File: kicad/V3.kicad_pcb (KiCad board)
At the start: 2 copper layers, 161.3 x 118.3 mm, 48 parts, among them U1 SuperMini nRF52840

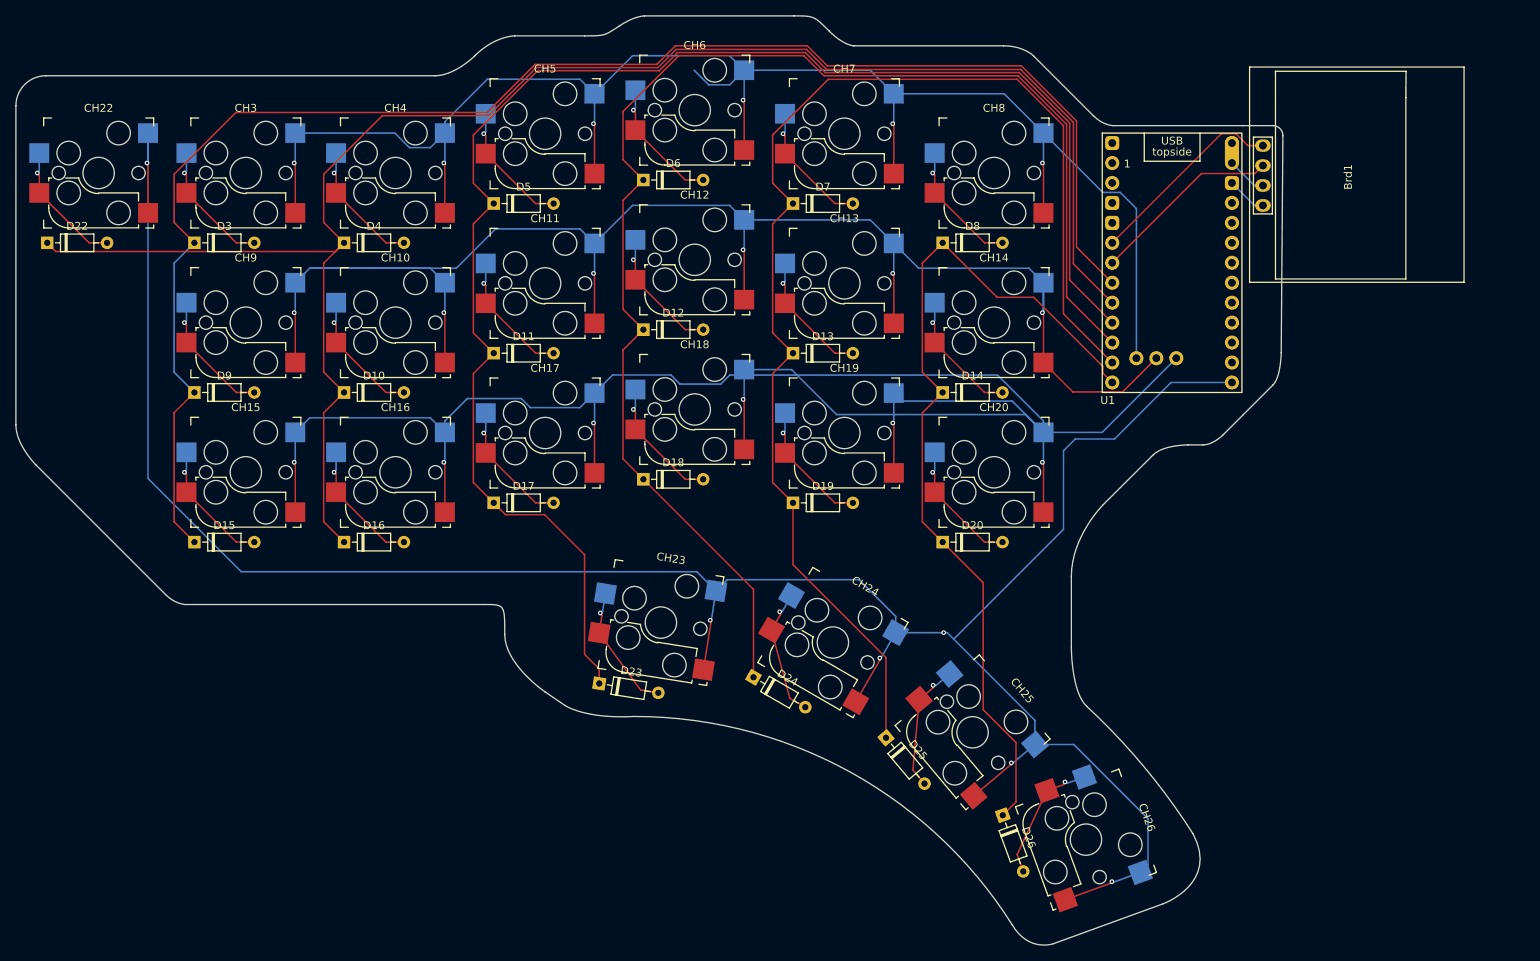
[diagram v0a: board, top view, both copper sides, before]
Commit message: change to esp32
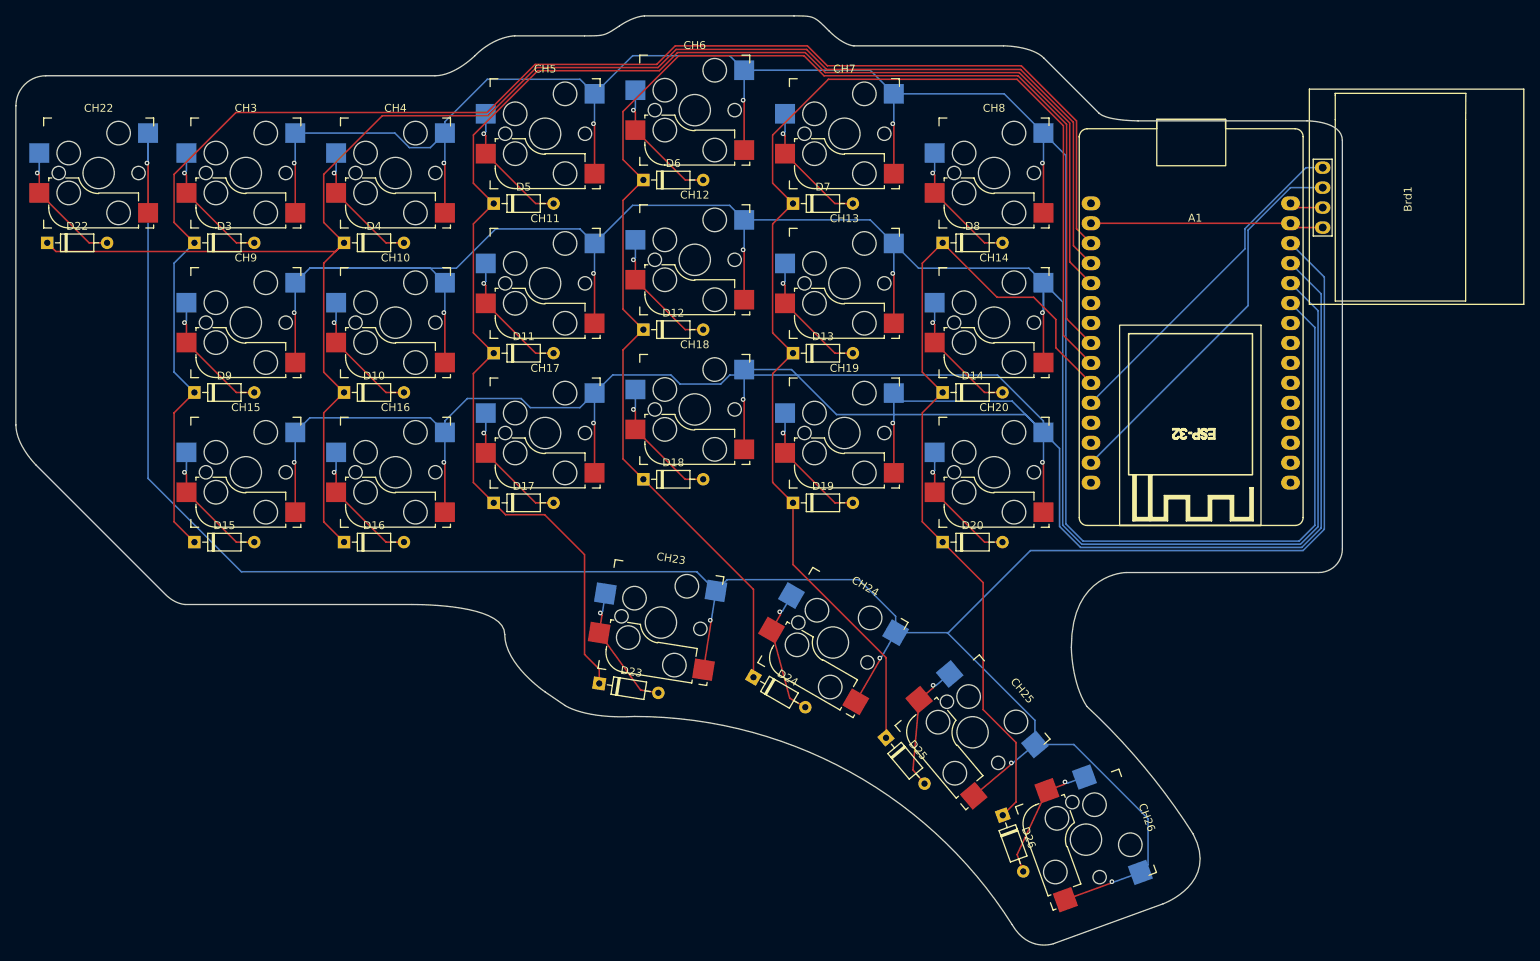
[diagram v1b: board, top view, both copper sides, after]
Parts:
- removed U1: SuperMini nRF52840, PCM_marbastlib-xp-promicroish:SuperMini_nRF52840_AH_USBup
- added A1: ESP32_DevKit_V1_DOIT_30GPIOs, PCM_SL_Development_Boards:DOIT_ESP32_DEVKIT_30Pins, F.Cu at (197.5, 64.5)
- moved Brd1 8.11 mm to (237.6, 64.0)
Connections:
- Brd1 pad 3: SDA -> SCL
- Brd1 pad 4: SDL -> SDA
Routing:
- net Row2: track 206.2 -> 287.2 mm
- net Row1: track 211.7 -> 282.9 mm
- net Row3: track 251.4 -> 314.2 mm
- net SCL: track 0.00 -> 49.6 mm
- net Row4: track 306.8 -> 343.7 mm, vias 6 -> 5
- net SDL: track 25.6 -> 0.00 mm
- net Earth: track 5.13 -> 29.7 mm
- net SDA: track 24.3 -> 43.4 mm
- net Col3: track 195.3 -> 189.2 mm
- net Col2: track 221.8 -> 215.6 mm
- net Col1: track 200.3 -> 194.1 mm
- net Col6: track 111.2 -> 110.1 mm
- net Col5: track 162.1 -> 161.1 mm
- net Col4: track 176.4 -> 175.4 mm
- net VCC: track 5.13 -> 4.32 mm
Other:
- board size 161.3 x 118.3 mm -> 168.9 x 118.3 mm

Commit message: problematic diodes
d2 and d34 cannot be used,d2 is the same pin as the builtin led, which
is used for serial confirmation rn, and d34 is input only
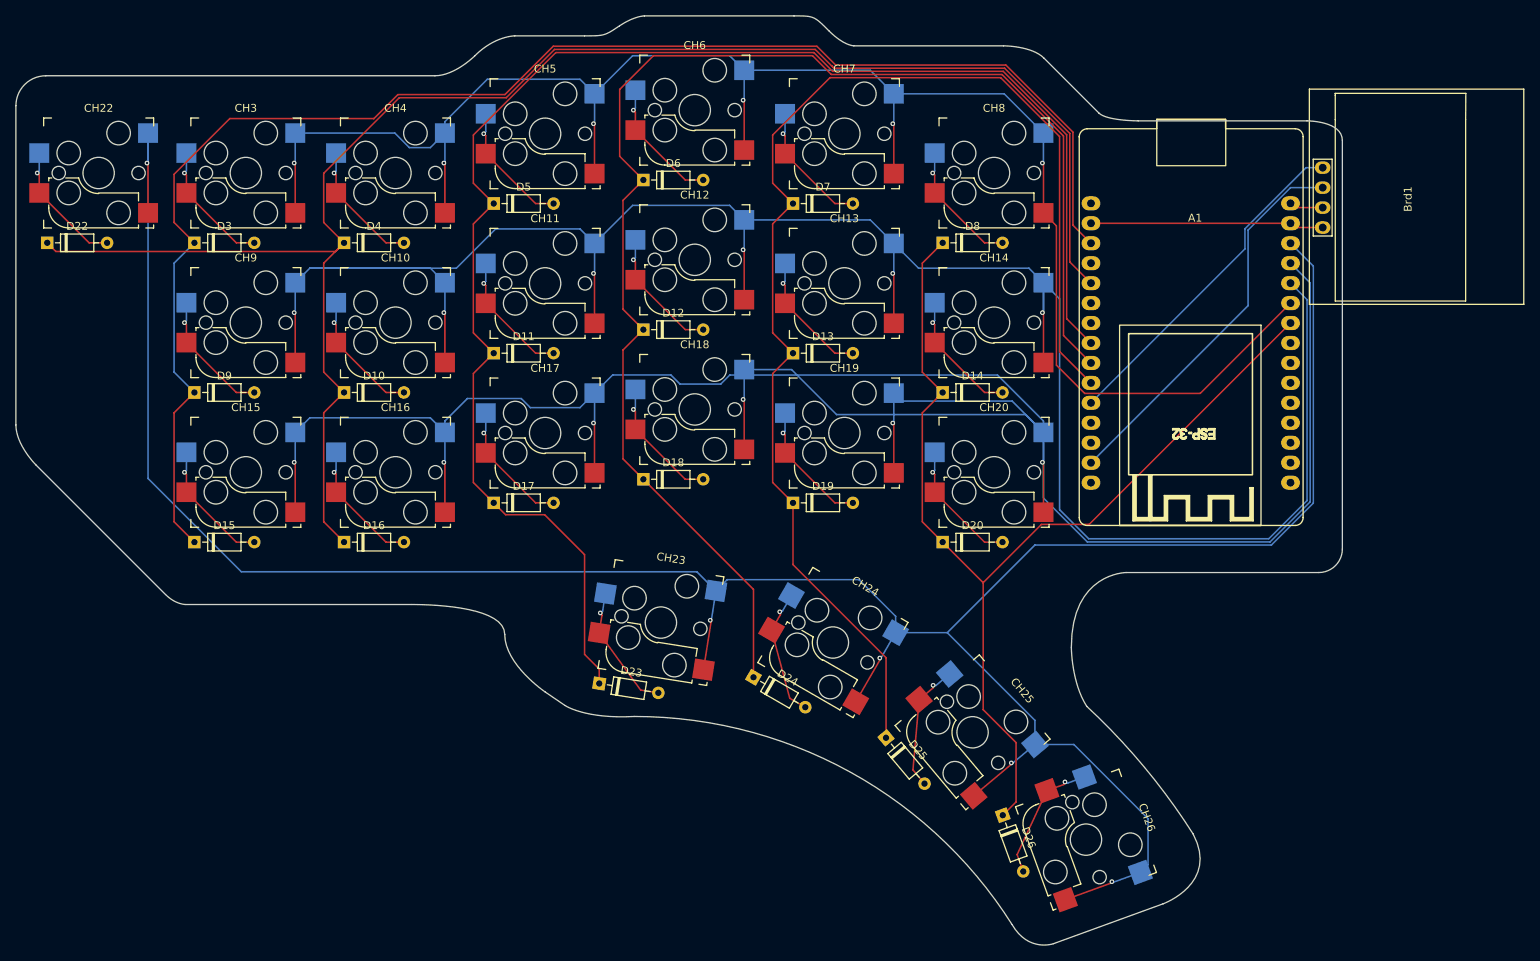
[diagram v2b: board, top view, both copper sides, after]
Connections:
- A1 pad 10: Col6 -> Col5
- A1 pad 24: unconnected-(A1-DAC2/ADC2_CH9/D26-Pad24) -> Col6
- A1 pad 4: Col2 -> unconnected-(A1-D2/ADC2_CH2-Pad4)
- A1 pad 5: Col3 -> Col2
- A1 pad 8: Col4 -> Col3
- A1 pad 9: Col5 -> Col4
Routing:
- net Row1: track 282.9 -> 225.1 mm
- net Col6: track 110.1 -> 134.5 mm
- net Col3: track 189.2 -> 195.7 mm
- net Row2: track 287.2 -> 281.8 mm
- net Row3: track 314.2 -> 308.8 mm
- net Row4: track 343.7 -> 339.7 mm
- net Col4: track 175.4 -> 179.0 mm
- net Col2: track 215.6 -> 217.3 mm
- net Col5: track 161.1 -> 162.7 mm
- net Col1: track 194.1 -> 193.0 mm

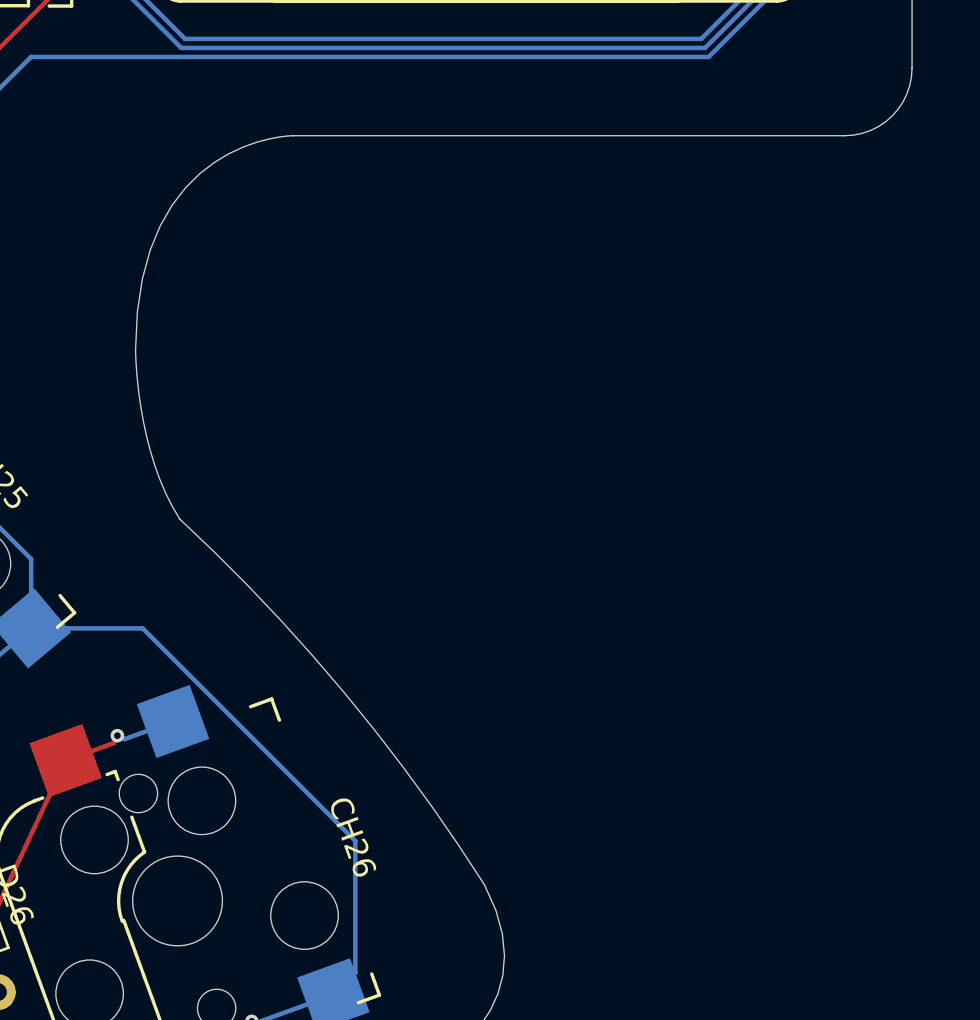
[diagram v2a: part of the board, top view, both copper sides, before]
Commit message: change from global to sheet labels
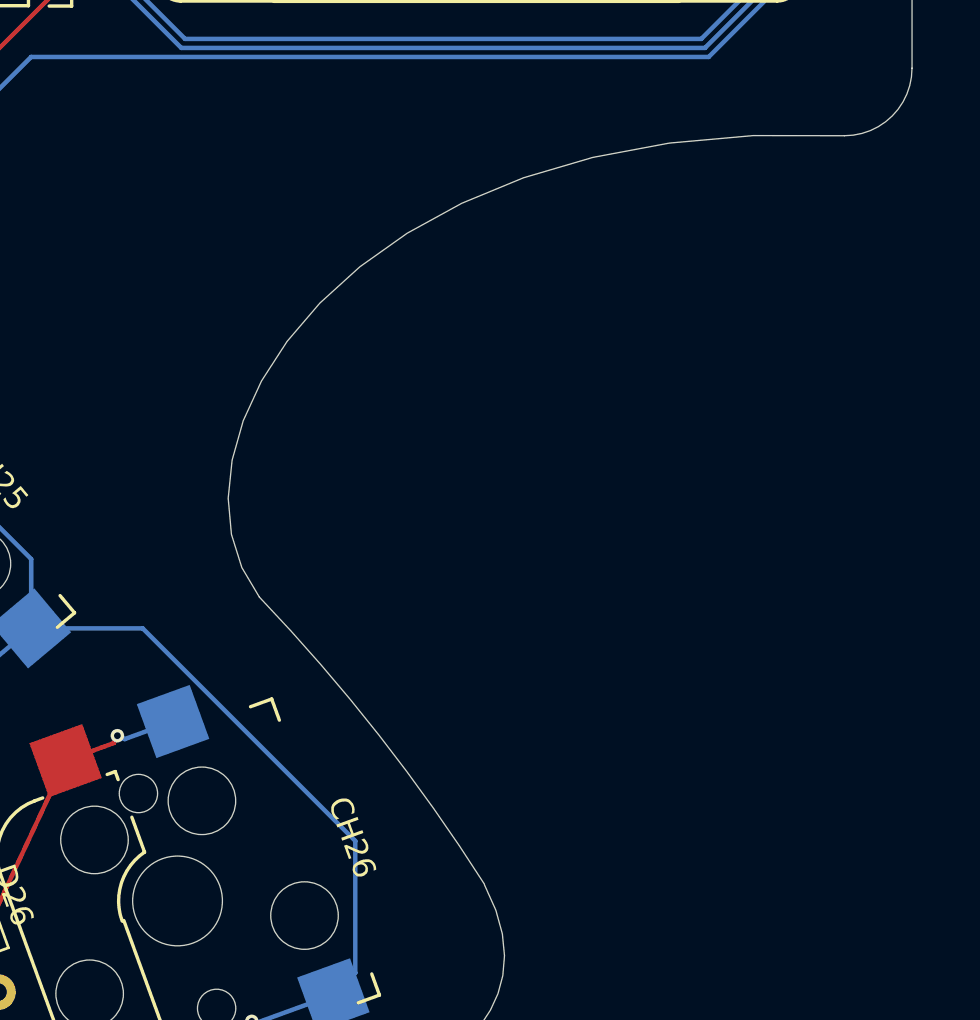
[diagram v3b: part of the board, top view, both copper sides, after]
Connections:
- net Col1 renamed /Col1
- net Col2 renamed /Col2
- net Col3 renamed /Col3
- net Col4 renamed /Col4
- net Col5 renamed /Col5
- net Col6 renamed /Col6
- net Row1 renamed /Row1
- net Row2 renamed /Row2
- net Row3 renamed /Row3
- net Row4 renamed /Row4
- A1 pad 11: SDA -> unconnected-(A1-D21/SDA-Pad11)
- A1 pad 14: SCL -> unconnected-(A1-D22/SCL-Pad14)
- Brd1 pad 3: SCL -> /SCL
- Brd1 pad 4: SDA -> /SDA
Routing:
- net (no net): track 0.00 -> 93.0 mm
- net SCL: track 49.6 -> 0.00 mm
- net SDA: track 43.4 -> 0.00 mm
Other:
- outline, holes or cut-outs redrawn

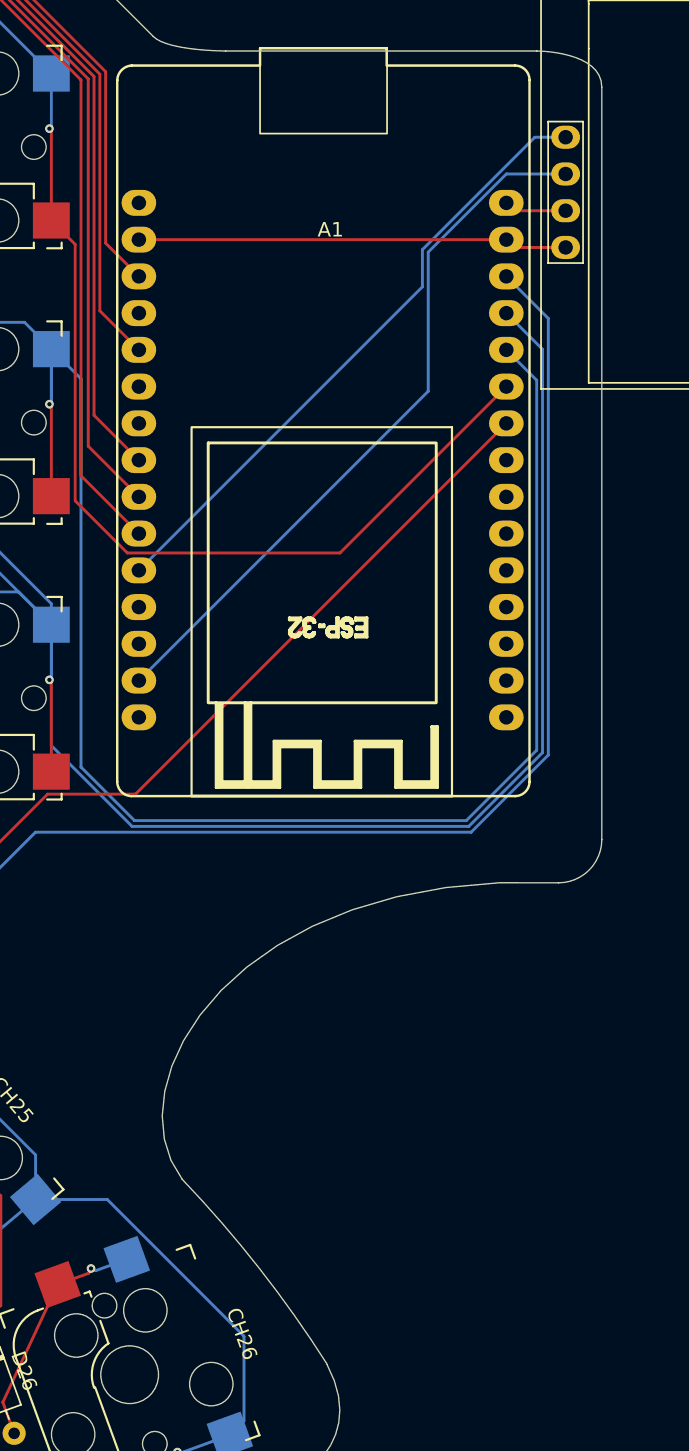
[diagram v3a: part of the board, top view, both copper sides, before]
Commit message: battery chargin module additon
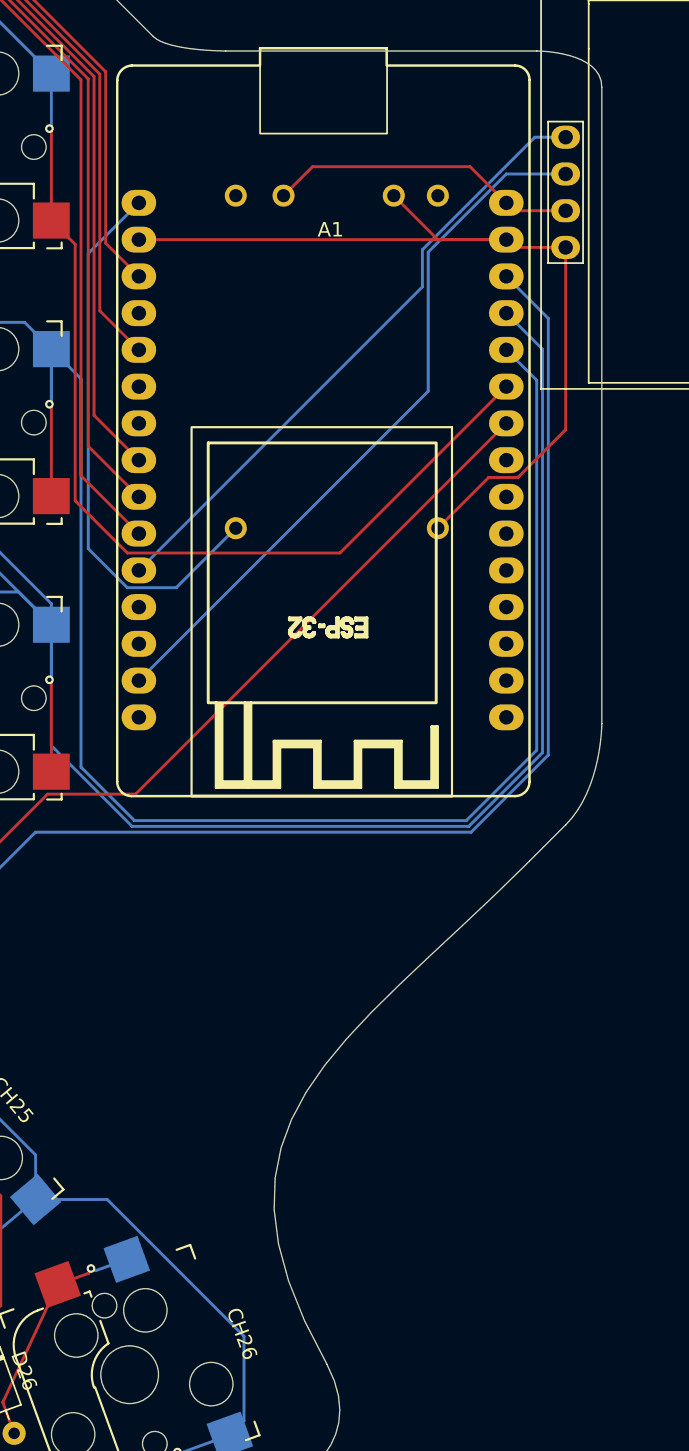
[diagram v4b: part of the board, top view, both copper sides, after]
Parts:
- added U1: ~, Library:HAYATEC TP4056 LIPO CHARGING MODULE, B.Cu at (211.1, 76.1)
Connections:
- A1 pad 1: unconnected-(A1-3.3V-Pad1) -> -3V3
- A1 pad 11: unconnected-(A1-D21/SDA-Pad11) -> /SDA
- A1 pad 14: unconnected-(A1-D22/SCL-Pad14) -> /SCL
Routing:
- net (no net): track 93.0 -> 0.00 mm
- net /SCL: track 0.00 -> 49.6 mm
- net /SDA: track 0.00 -> 43.4 mm
- net -3V3: track 0.00 -> 38.4 mm
- net Earth: track 29.7 -> 63.0 mm
- net VCC: track 4.32 -> 21.6 mm
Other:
- outline, holes or cut-outs redrawn

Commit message: usp+uart converter
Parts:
- added U2: ~, Library:CH340C_pins, F.Cu at (191.0, 117.0)
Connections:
- A1 pad 12: unconnected-(A1-RX0/GPIO3-Pad12) -> /RX
- A1 pad 13: unconnected-(A1-TX0/GPIO1-Pad13) -> /TX
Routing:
- net Earth: track 63.0 -> 142.2 mm
- net /TX: track 0.00 -> 35.2 mm, vias 0 -> 2
- net /RX: track 0.00 -> 31.9 mm, vias 0 -> 2
- net -3V3: track 38.4 -> 60.1 mm, vias 0 -> 3

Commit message: switch
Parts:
- added SW1: Slide_Switch_SPDT_P3mm_10x5x10mm, PCM_SL_Devices:Slide_Switch_SPDT_P3mm_10x5x10mm, F.Cu at (230.0, 97.5)
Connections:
- U1 pad 1: -3V3 -> Net-(U1-Out+)
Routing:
- net -3V3: track 60.1 -> 50.9 mm
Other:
- board size 168.9 x 118.3 mm -> 172.9 x 118.3 mm
